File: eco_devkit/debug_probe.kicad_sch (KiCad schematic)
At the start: 0 parts

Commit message: added modules footprint and digikey datasheets & schematic adjustments
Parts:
- added C1, C4: 10u, Capacitor_SMD:C_0402_1005Metric, symbol Device:C_Small
- added C10, C8: 1u, Capacitor_SMD:C_0402_1005Metric, symbol Device:C_Small
- added C11, C12, C13, C14, C15, C16, C5, C6, C7, C9: 100n, Capacitor_SMD:C_0402_1005Metric, symbol Device:C_Small
- added C2, C3: 15p, Capacitor_SMD:C_0402_1005Metric, symbol Device:C_Small
- added J1: Conn_01x06_Pin, Connector_PinSocket_2.54mm:PinSocket_1x06_P2.54mm_Vertical, symbol Connector:Conn_01x06_Pin
- added J2: USB_C_Receptacle_USB2.0_16P, Connector_USB:USB_C_Receptacle_HCTL_HC-TYPE-C-16P-01A, symbol Connector:USB_C_Receptacle_USB2.0_16P
- added MEM1: ~, Footprint-FlashMEM:SOIC127P790X216-8N, symbol PROBE-SYMBOL-LIB:RP2040_Flash_MEM
- added PWR1: ~, Footprint-NP1117-POWER-SUPPLY:SOT230P700X175-4N, symbol PROBE-SYMBOL-LIB:NCP1117-3.3SOT_223
- added R2: DNF, Resistor_SMD:R_0402_1005Metric, symbol Device:R_Small
- added R3, R4: 27, Resistor_SMD:R_0402_1005Metric, symbol Device:R_Small
- added R5: 1k, Resistor_SMD:R_0402_1005Metric, symbol Device:R_Small
- added U1: ~, Package_DFN_QFN:QFN-56-1EP_7x7mm_P0.4mm_EP3.2x3.2mm_ThermalVias, symbol PROBE-SYMBOL-LIB:RP2040
- added Y1: ABM8-272-T3, ABM8_272_T3:XTAL_ABM8-272-T3, symbol Device:Crystal_GND24
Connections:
- new net: R3.1, U1.47 (USB_DP)
- new net: MEM1.1 (QSPI_SS), R2.1
- new net: C3.1, R5.1, Y1.3
- new net: R4.1, U1.46 (USB_DM)
- new net +1V1: C6.1, C7.1, C8.1, U1.23 (DVDD), U1.45 (VREG_VOUT), U1.50 (DVDD)
- new net +3V3: C10.1, C11.1, C12.1, C13.1, C14.1, C15.1, C16.1, C4.1, C5.1, C9.1, J1.1 (Pin_1), MEM1.8 (VCC), PWR1.2 (VO), R2.2, U1.1 (IOVDD), U1.10 (IOVDD), U1.22 (IOVDD), U1.33 (IOVDD), U1.42 (IOVDD), U1.43 (ADC_AVDD), U1.44 (VREG_IN), U1.48 (USB_VDD), U1.49 (IOVDD)
- new net GND: C1.2, C10.2, C11.2, C12.2, C13.2, C14.2, C15.2, C16.2, C2.1, C3.2, C4.2, C5.2, C6.2, C7.2, C8.2, C9.2, J1.3 (Pin_3), J2.A1 (GND), J2.A12 (GND), J2.B1 (GND), J2.B12 (GND), J2.S1 (SHIELD), MEM1.4 (GND), PWR1.1 (GND), U1.19 (TESTN), U1.57 (GND), Y1.2, Y1.4
- new net QSPI_SCLK: U1.52 (QSPI_SCLK)
- new net QSPI_SS: U1.56 (QSPI_SS)
- new net RP2040_GPIO2: U1.4 (GPIO2)
- new net RP2040_GPIO3: U1.5 (GPIO3)
- new net RP2040_GPIO4: U1.6 (GPIO4)
- new net RP2040_GPIO5: U1.7 (GPIO5)
- new net RP2040_USB_D+: J2.A6 (D+), R3.2
- new net RP2040_USB_D-: J2.A7 (D-), R4.2
- new net SD0: U1.53 (SD0)
- new net SD1: U1.55 (SD1)
- new net SD2: U1.54 (SD2)
- new net SD3: U1.51 (SD3)
- new net SWCLK: J1.2 (Pin_2), U1.24 (SWCLK)
- new net SWDIO: J1.4 (Pin_4), U1.25 (SWDIO)
- new net VBUS: C1.1, J2.A4 (VBUS), J2.A9 (VBUS), J2.B4 (VBUS), J2.B9 (VBUS), PWR1.3 (VI)
- new net XIN: C2.2, U1.20 (XIN), Y1.1
- new net XOUT: R5.2, U1.21 (XOUT)
- no-connect marks 0 -> 39

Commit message: Update layout
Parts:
- removed C1, C4: 10u, Capacitor_SMD:C_0402_1005Metric, symbol Device:C_Small
- removed C10, C8: 1u, Capacitor_SMD:C_0402_1005Metric, symbol Device:C_Small
- removed C11, C12, C13, C14, C15, C16, C5, C6, C7, C9: 100n, Capacitor_SMD:C_0402_1005Metric, symbol Device:C_Small
- removed C3: 15p, Capacitor_SMD:C_0402_1005Metric, symbol Device:C_Small
- removed J2: USB_C_Receptacle_USB2.0_16P, Connector_USB:USB_C_Receptacle_HCTL_HC-TYPE-C-16P-01A, symbol Connector:USB_C_Receptacle_USB2.0_16P
- removed PWR1: ~, Footprint-NP1117-POWER-SUPPLY:SOT230P700X175-4N, symbol PROBE-SYMBOL-LIB:NCP1117-3.3SOT_223
- removed R4: 27, Resistor_SMD:R_0402_1005Metric, symbol Device:R_Small
- removed R5: 1k, Resistor_SMD:R_0402_1005Metric, symbol Device:R_Small
- added C27: 15p, Capacitor_SMD:C_0603_1608Metric, symbol Device:C_Small
- added C28, C30, C31, C33, C35, C36, C37, C38, C39, C40: 100n, Capacitor_SMD:C_0402_1005Metric, symbol Device:C_Small
- added C29: 10u, Capacitor_SMD:C_0402_1005Metric, symbol Device:C_Small
- added C32, C34: 1u, Capacitor_SMD:C_0402_1005Metric, symbol Device:C_Small
- added D8: SB120, Diode_SMD:D_SOD-123F, symbol Diode:SB120
- added J8: USB_C_Receptacle_USB2.0_16P, lib:UJ20-C-H-G-SMT-1-P16-TR, symbol Connector:USB_C_Receptacle_USB2.0_16P
- added R36, R37: 5.1k, Resistor_SMD:R_0402_1005Metric, symbol Device:R_Small_US
- added R38: 1k, Resistor_SMD:R_0402_1005Metric, symbol Device:R_Small_US
- added R39: 10k, Resistor_SMD:R_0402_1005Metric, symbol Device:R_Small_US
- added R41: 27, Resistor_SMD:R_0402_1005Metric, symbol Device:R_Small_US
- C26: renamed from C2; footprint Capacitor_SMD:C_0402_1005Metric -> Capacitor_SMD:C_0603_1608Metric; MPN (none) -> C0603C150K8RACAUTO
- J9: renamed from J1; value Conn_01x06_Pin -> SWD Interface
- MEM1: value ~ -> AT25EU0011A-SSHN-T; MPN (none) -> AT25EU0011A-SSHN-T
- R40: renamed from R3; symbol Device:R_Small -> Device:R_Small_US; MPN (none) -> RCS040227R0FKED
- U1: value ~ -> RP2040
- Y2: renamed from Y1; footprint ABM8_272_T3:XTAL_ABM8-272-T3 -> lib:ABM8-272-T3; MPN (none) -> ABM8-272-T3
- renumbered R2 to R35
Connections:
- net +1V1: now also C30.1, C31.1, C32.2
- net +3V3: now also C28.1, C33.1, C34.2, C35.1, C36.1, C37.1, C38.1, C39.1, C40.1, R39.1
- net GND: now also C27.1, C28.2, C29.2, C30.2, C31.2, C32.1, C33.2, C34.1, C35.2, C36.2, C37.2, C38.2, C39.2, C40.2, J8.A1 (GND), J8.A12 (GND), J8.B1 (GND), J8.B12 (GND), R36.2, R37.2
- net QSPI_SCLK: now also MEM1.6 (QSPI_SCLK)
- net QSPI_SS: now also MEM1.1 (QSPI_SS), R35.1
- net RP2040_USB_D+: now also J8.A6 (D+), J8.B6 (D+)
- net RP2040_USB_D-: now also J8.A7 (D-), J8.B7 (D-), R41.2
- net SD0: now also MEM1.5 (QSPI_SDO)
- net SD1: now also MEM1.2 (QSPI_SD1)
- net SD2: now also MEM1.3 (QSPI_SD2)
- net SD3: now also MEM1.7 (QSPI_SD3)
- net XOUT: now also R38.2
- net RESET: now reaches J9.5 (Pin_5)
- net RESET: now also U1.26 (RUN), R39.2
- net at Y2.3: now also C27.2, R38.1
- net at U1.46 (USB_DM): now also R41.1
- net RP2040_GPIO2 renamed PROBE_GPIO2/SWCLK
- net RP2040_GPIO3 renamed POBRE_GPIO3/SWDIO
- net RP2040_GPIO4 renamed PROBE_GPIO4/UART_TX
- net RP2040_GPIO5 renamed POBRE_GPIO5/UART_RX
- new net: J8.A5 (CC1), R36.1
- new net: J8.B5 (CC2), R37.1
- new net: D8.2 (A), J8.A4 (VBUS), J8.A9 (VBUS), J8.B4 (VBUS), J8.B9 (VBUS)
- new net +VBUS: C29.1, D8.1 (K)
- no-connect marks 39 -> 30
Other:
- note added: "RP2040 CRYSTAL MODULE"
- note added: "RP2040 DEBUG PROBE"
- note added: "RP2040 FLASH MODULE"
- note added: "RP2040 PICOPROBE"
- note added: "RP2040 USB MODULE"
- moved on the sheet: C26, J9, MEM1, R35

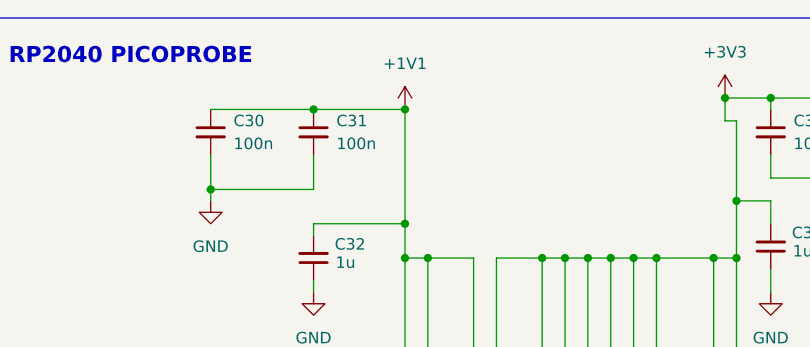
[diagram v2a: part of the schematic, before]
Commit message: routed all components except header and copper pours
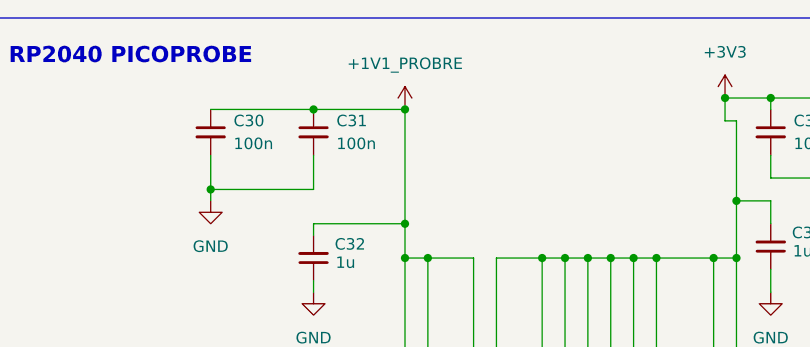
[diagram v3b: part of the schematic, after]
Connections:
- net +1V1 renamed +1V1_PROBRE
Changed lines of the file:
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@@
 			)
 		)
-		(property "Value" "+1V1"
+		(property "Value" "+1V1_PROBRE"
 			(at 173.99 19.05 0)
 			(effects
